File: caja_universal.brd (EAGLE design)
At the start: 137.8 x 101.5 mm, 40 parts, among them IC1 AD711N, IC2 AD620N, IC3 TL084P, IC4 TL084P, IC5 AD711N, IC6 TL084P

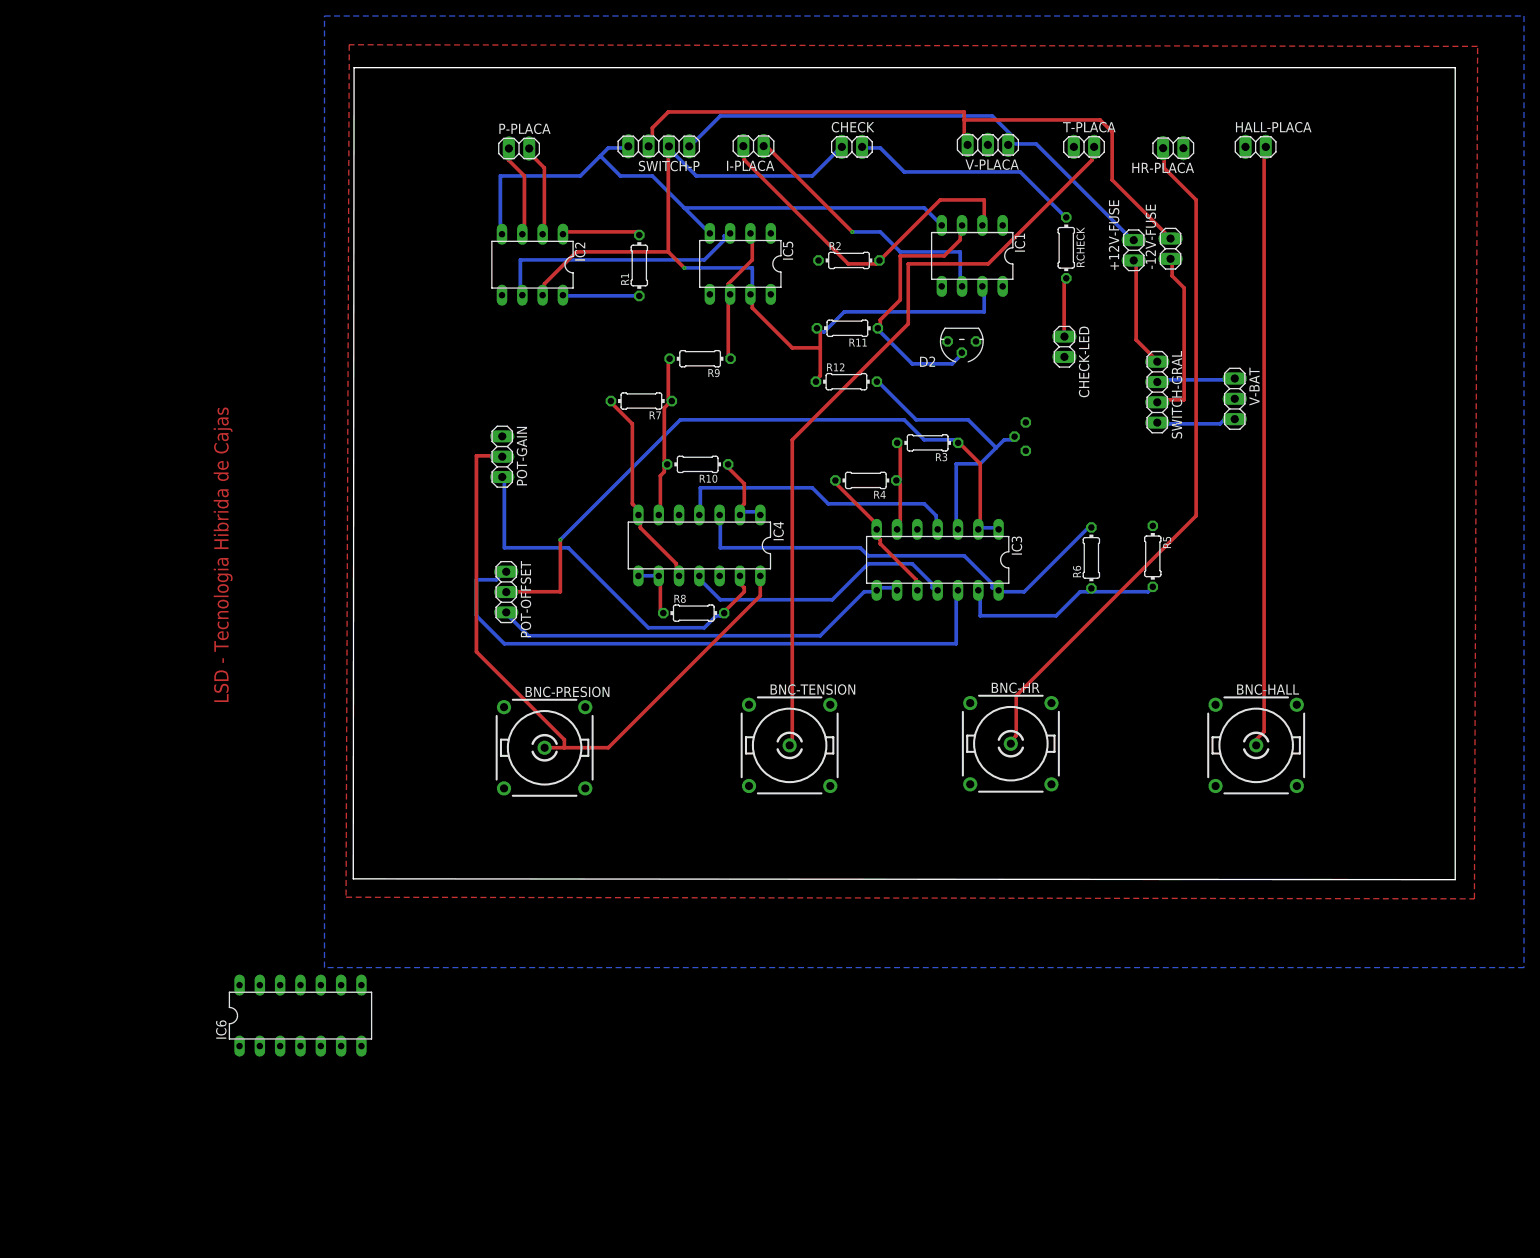
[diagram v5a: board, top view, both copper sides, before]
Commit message: corregimos alimentacion TL084
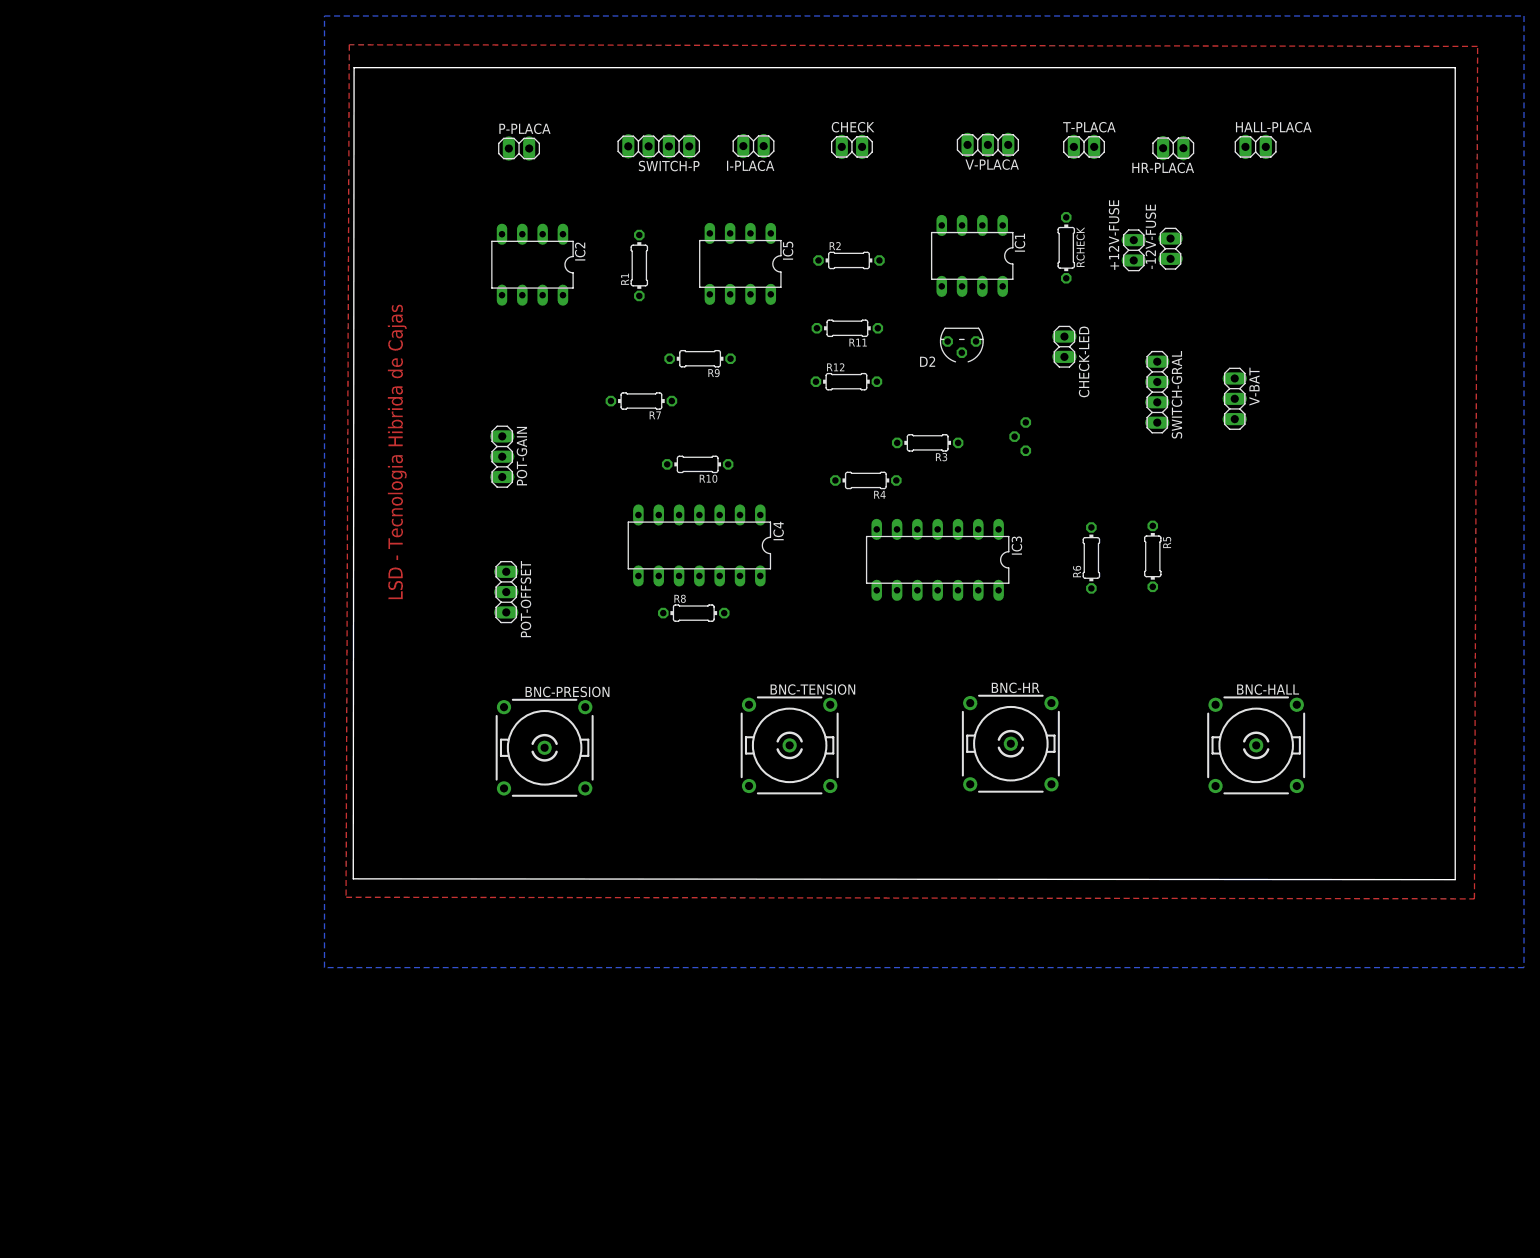
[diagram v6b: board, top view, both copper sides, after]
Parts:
- removed IC6: TL084P, linear:DIL14
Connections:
- removed net +12V-PRESION: CHECK.1, IC1.7, IC2.7, IC5.7, R11.2, R12.1, SWITCH-P.2
- removed net -12V-PRESION: IC1.4, IC2.4, IC5.4, SWITCH-P.4
- net V+: now also CHECK.1, IC1.7, IC2.7, IC5.7, R11.2, R12.1, SWITCH-P.2; no longer IC6.4
- net V-: now also IC1.4, IC2.4, IC5.4, SWITCH-P.4; no longer IC6.11
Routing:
- net +12V-PRESION: track 116.3 -> 0.00 mm, vias 1 -> 0
- net TENSION: track 96.6 -> 0.00 mm
- net HR: track 85.8 -> 0.00 mm
- net 1.25V: track 85.3 -> 0.00 mm, vias 1 -> 0
- net -12V: track 82.3 -> 0.00 mm
- net POUT: track 81.6 -> 0.00 mm
- net OFFSET: track 76.9 -> 0.00 mm
- net -12V-PRESION: track 75.6 -> 0.00 mm
- net HALL: track 75.4 -> 0.00 mm
- net +12V: track 65.3 -> 0.00 mm
- net N$11: track 56.4 -> 0.00 mm
- net -1.25V: track 52.9 -> 0.00 mm
- net N$16: track 47.2 -> 0.00 mm
- net -I: track 43.8 -> 0.00 mm
- net V+: track 36.1 -> 0.00 mm
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
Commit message: Corregimos placa de conexion universal y mochila
Esta version se envia a imprimir
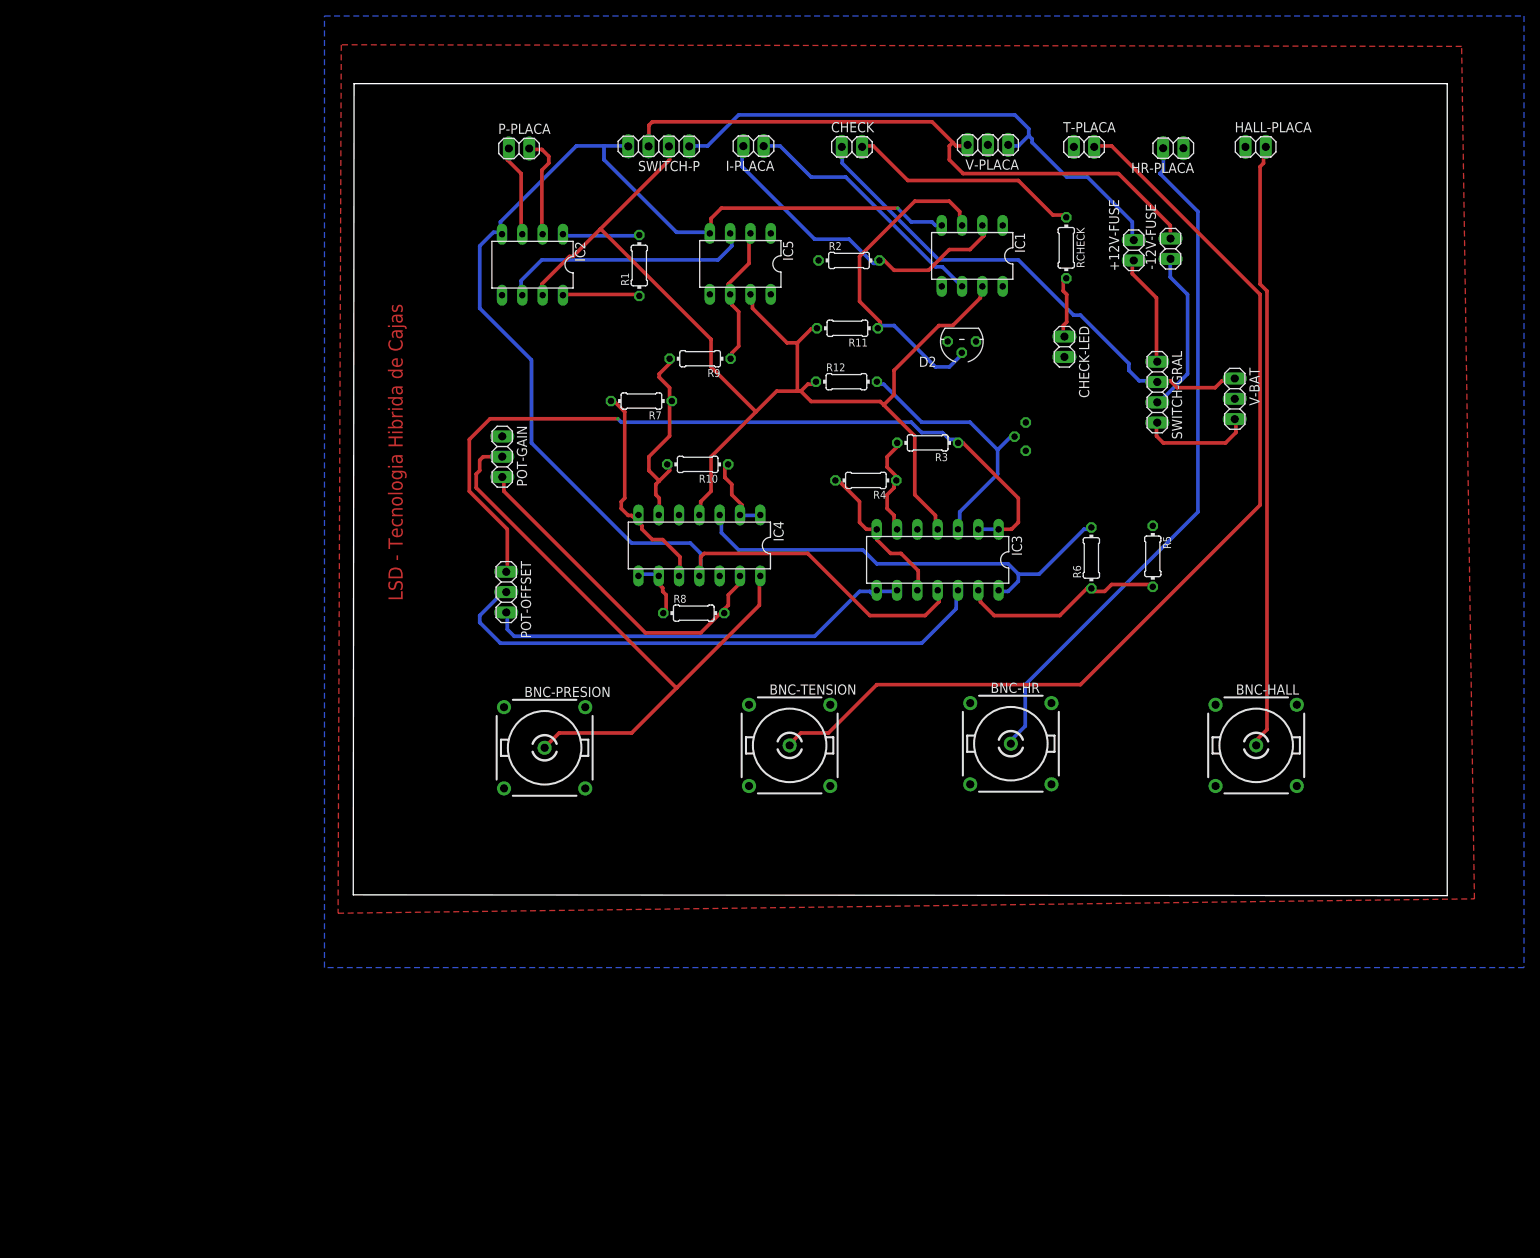
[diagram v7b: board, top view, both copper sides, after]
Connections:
- net +12VBAT: now also CHECK.1
- net 1.25V: now also POT-OFFSET.1; no longer POT-OFFSET.2
- net OFFSET: now also POT-OFFSET.2; no longer POT-OFFSET.1
- net V+: no longer CHECK.1
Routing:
- net V-: track 0.00 -> 170.7 mm, vias 0 -> 1
- net V+: track 0.00 -> 150.6 mm
- net TENSION: track 0.00 -> 126.6 mm
- net 1.25V: track 0.00 -> 100.9 mm, vias 0 -> 1
- net HR: track 0.00 -> 86.8 mm
- net POUT: track 0.00 -> 80.6 mm
- net -12V: track 0.00 -> 79.0 mm
- net HALL: track 0.00 -> 76.4 mm
- net OFFSET: track 0.00 -> 70.3 mm
- net +12V: track 0.00 -> 68.8 mm
- net +12VBAT: track 0.00 -> 63.9 mm
- net N$11: track 0.00 -> 57.2 mm
- net -1.25V: track 0.00 -> 54.1 mm
- net N$16: track 0.00 -> 43.4 mm
- net N$3: track 0.00 -> 42.0 mm
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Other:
- board size 137.8 x 101.5 mm -> 136.8 x 101.5 mm

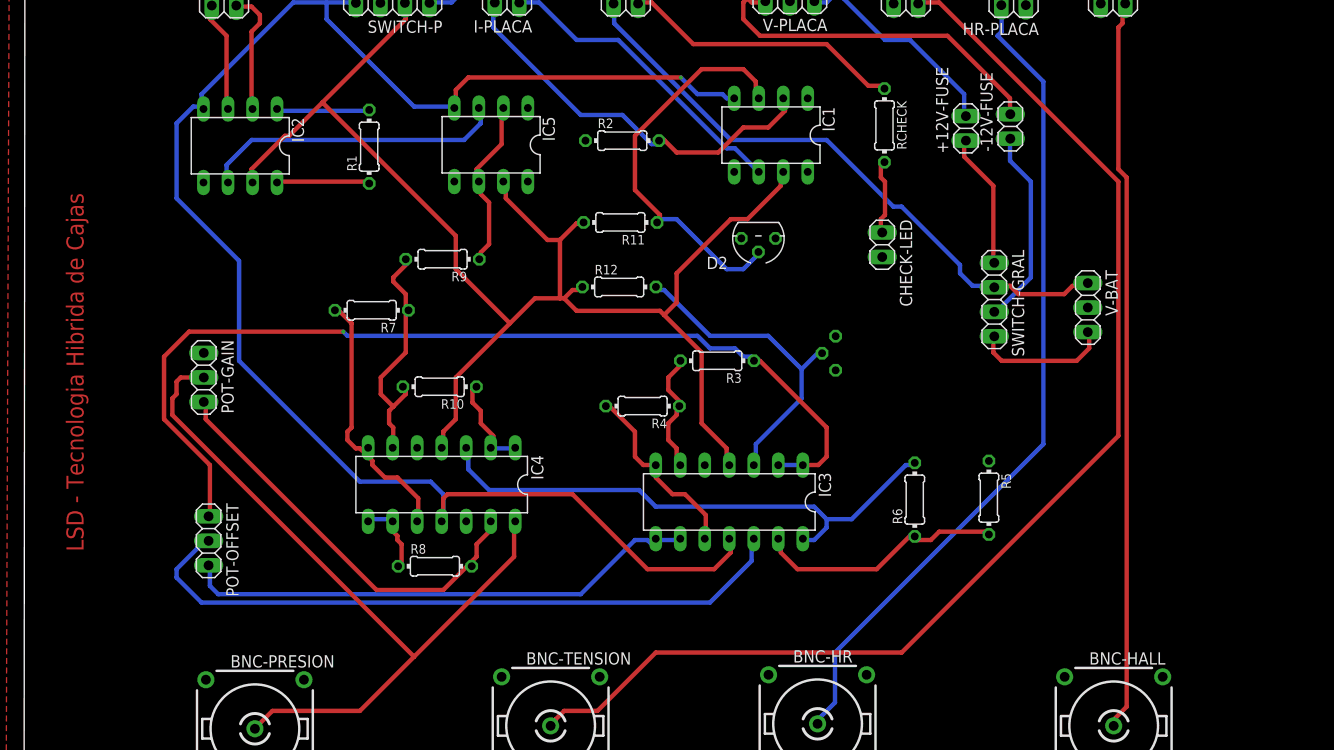
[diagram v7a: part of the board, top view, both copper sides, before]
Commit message: Cambios minimos caja, update libreria conector para mochila
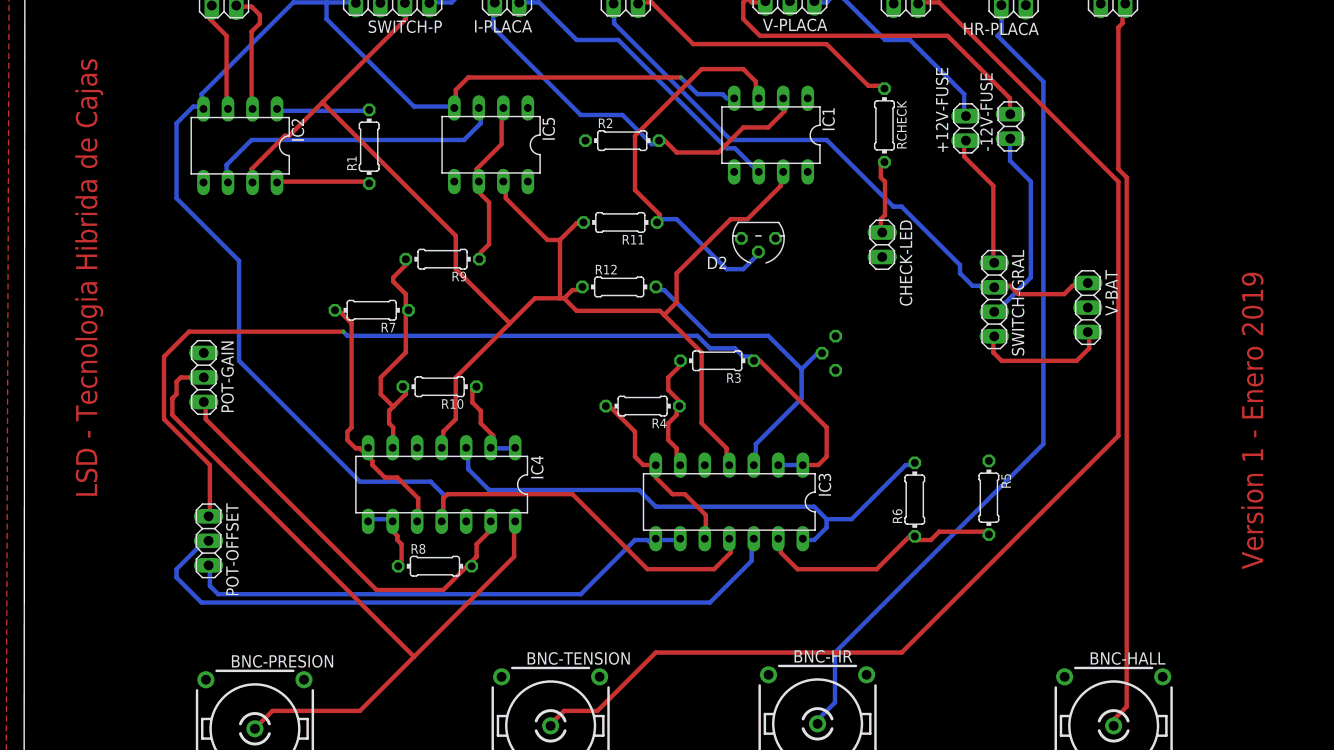
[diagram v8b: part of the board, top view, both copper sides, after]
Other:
- board text added: "Version 1 - Enero 2019"
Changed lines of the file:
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@@
 <wire x1="118.4" y1="88.54" x2="-18.3" y2="88.54" width="0" layer="20"/>
 <wire x1="-18.3" y1="88.54" x2="-18.4" y2="-12.9" width="0" layer="20"/>
-<text x="-14" y="61" size="1.778" layer="1" rot="R270">LSD - Tecnologia Hibrida de Cajas</text>
+<text x="-13" y="75" size="2.1844" layer="1" font="vector" rot="R270">LSD - Tecnologia Hibrida de Cajas</text>
+<text x="110" y="22" size="2.1844" layer="1" font="vector" rot="R90">Version 1 - Enero 2019</text>
 </plain>
 <attributes>
